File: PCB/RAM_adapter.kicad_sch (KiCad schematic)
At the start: 13 parts, among them J1 #WR, J2 DB25_Plug, U1 HM62256BLP, U2 74LS573

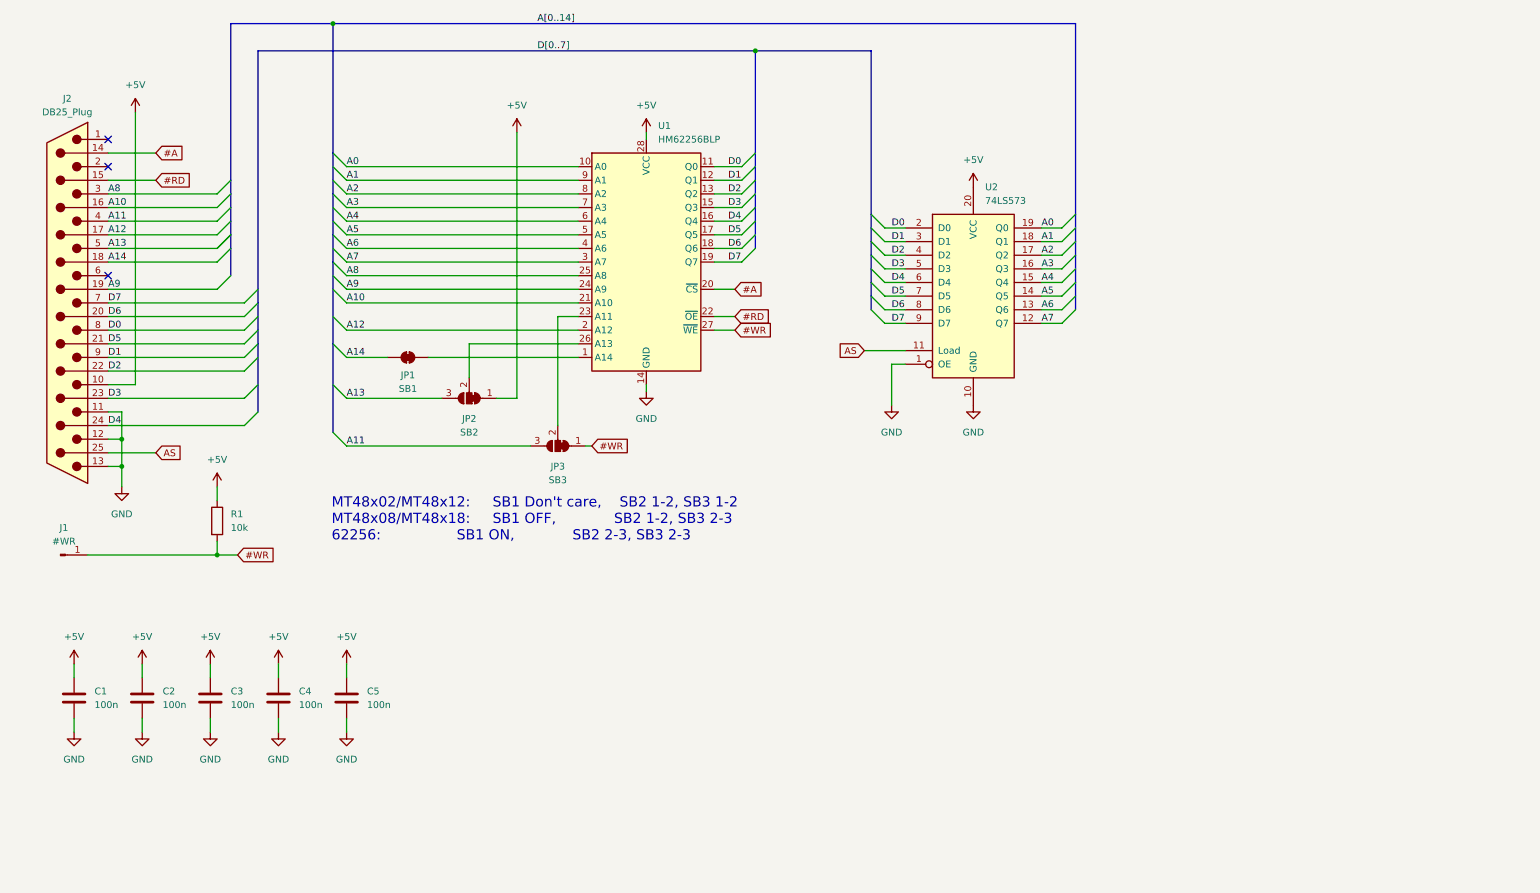
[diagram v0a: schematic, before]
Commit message: Revised RAM adapter PCB
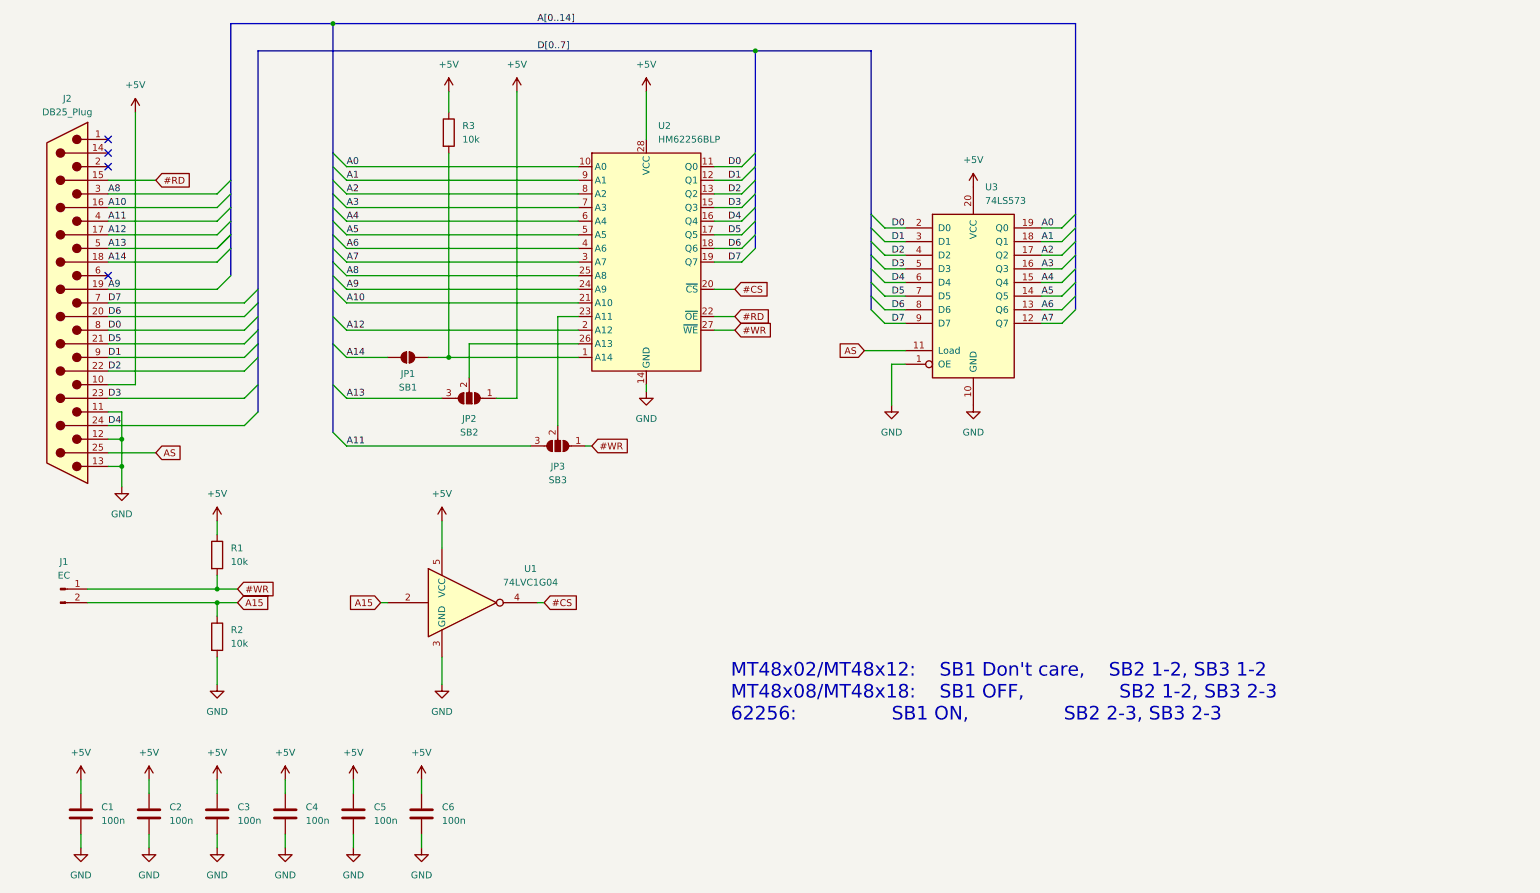
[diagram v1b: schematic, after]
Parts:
- removed J1: #WR, Connector_PinHeader_2.54mm:PinHeader_1x01_P2.54mm_Vertical, symbol Connector:Conn_01x01_Pin
- removed JP1: SB1, Jumper:SolderJumper-2_P1.3mm_Bridged_RoundedPad1.0x1.5mm, symbol Jumper:SolderJumper_2_Bridged
- removed JP2: SB2, Jumper:SolderJumper-3_P1.3mm_Bridged12_RoundedPad1.0x1.5mm_NumberLabels, symbol Jumper:SolderJumper_3_Bridged12
- removed JP3: SB3, Jumper:SolderJumper-3_P1.3mm_Bridged12_RoundedPad1.0x1.5mm_NumberLabels, symbol Jumper:SolderJumper_3_Bridged12
- added C6: 100n, Capacitor_SMD:C_1206_3216Metric_Pad1.33x1.80mm_HandSolder, symbol Device:C
- added J1: EC, Connector_PinHeader_2.54mm:PinHeader_1x02_P2.54mm_Vertical, symbol Connector:Conn_01x02_Pin
- added JP1: SB1, Jumper:SolderJumper-2_P1.3mm_Open_RoundedPad1.0x1.5mm, symbol Jumper:SolderJumper_2_Open
- added JP2: SB2, Jumper:SolderJumper-3_P1.3mm_Open_RoundedPad1.0x1.5mm, symbol Jumper:SolderJumper_3_Open
- added JP3: SB3, Jumper:SolderJumper-3_P1.3mm_Open_RoundedPad1.0x1.5mm, symbol Jumper:SolderJumper_3_Open
- added R2, R3: 10k, Resistor_SMD:R_1206_3216Metric_Pad1.30x1.75mm_HandSolder, symbol Device:R
- added U1: 74LVC1G04, Package_TO_SOT_SMD:SOT-23-5_HandSoldering, symbol 74xGxx:74LVC1G04
- U2: renamed from U1; footprint Package_DIP:DIP-28_W15.24mm -> Socket:DIP_Socket-28_W11.9_W12.7_W15.24_W17.78_W18.5_3M_228-1277-00-0602J
- renumbered U2 to U3
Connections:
- net #WR: now also J1.1 (Pin_1), JP3.1 (A)
- net +5V: now also C6.1, JP2.1 (A), R3.1, U1.5 (VCC)
- net A11: now also JP3.3 (B)
- net A13: now also JP2.3 (B)
- net A14: now also JP1.2 (B)
- net GND: now also C6.2, R2.2, U1.3 (GND)
- net at U2.26 (A13): now also JP2.2 (C)
- net at U2.1 (A14): now also JP1.1 (A), R3.2
- net at U2.23 (A11): now also JP3.2 (C)
- net #A: no longer names the net of J2.14 (P14)
- net #A: no longer U2.20 (~{CS})
- new net #CS: U1.4, U2.20 (~{CS})
- new net A15: J1.2 (Pin_2), R2.1, U1.2
- no-connect marks 3 -> 4
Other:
- moved on the sheet: C1, C2, C3, C4, C5, R1

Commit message: ROM reader project PCBs updated
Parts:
- added D1: Schottky, Diode_SMD:D_SMB_Handsoldering, symbol Device:D_Schottky
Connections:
- net +5V: now also D1.1 (K)
- net GND: now also D1.2 (A)
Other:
- note added: "M48x02/M48x12: SB1 OFF, SB2 1-2, SB3 1-2 M48x08/M48x18: SB1 OFF, SB2 1-2, SB3 2-3 62256: SB1 ON, SB2 2-3, SB3 2-3"
- note removed: "MT48x02/MT48x12: SB1 Don't care, SB2 1-2, SB3 1-2 MT48x08/MT48x18: SB1 OFF, SB2 1-2, SB3 2-3 62256: SB1 ON, SB2 2-3, SB3 2-3"
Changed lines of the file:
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@@
 		)
 	)
+	(wire
+		(pts
+			(xy 129.54 170.18) (xy 129.54 172.72)
+		)
+		(stroke
+			(width 0)
+			(type default)
+		)
+	)
 	(bus
 		(pts
@@
 		)
 	)
+	(wire
+		(pts
+			(xy 129.54 180.34) (xy 129.54 182.88)
+		)
+		(stroke
+			(width 0)
+			(type default)
+		)
+	)
 	(bus
 		(pts
@@
 		)
 	)
-	(text "MT48x02/MT48x12:	SB1 Don't care,	SB2 1-2, SB3 1-2\nMT48x08/MT48x18:	SB1 OFF,				SB2 1-2, SB3 2-3\n62256:				SB1 ON,				SB2 2-3, SB3 2-3"
+	(text "M48x02/M48x12:	SB1 OFF,	SB2 1-2, SB3 1-2\nM48x08/M48x18:	SB1 OFF,	SB2 1-2, SB3 2-3\n62256:			SB1 ON,	SB2 2-3, SB3 2-3"
 		(exclude_from_sim no)
-		(at 171.958 153.924 0)
+		(at 187.452 155.194 0)
 		(effects
 			(font
@@
 	)
 	(symbol
+		(lib_name "GND_1")
+		(lib_id "power:GND")
+		(at 129.54 182.88 0)
+		(unit 1)
+		(exclude_from_sim no)
+		(in_bom yes)
+		(on_board yes)
+		(dnp no)
+		(fields_autoplaced yes)
+		(property "Reference" "#PWR027"
+			(at 129.54 189.23 0)
+			(effects
+				(font
+					(size 1.27 1.27)
+				)
+				(hide yes)
+			)
+		)
+		(property "Value" "GND"
+			(at 129.54 187.96 0)
+			(effects
+				(font
+					(size 1.27 1.27)
+				)
+			)
+		)
+		(property "Footprint" ""
+			(at 129.54 182.88 0)
+			(effects
+				(font
+					(size 1.27 1.27)
+				)
+				(hide yes)
+			)
+		)
+		(property "Datasheet" ""
+			(at 129.54 182.88 0)
+			(effects
+				(font
+					(size 1.27 1.27)
+				)
+				(hide yes)
+			)
+		)
+		(property "Description" "Power symbol creates a global label with name \"GND\" , ground"
+			(at 129.54 182.88 0)
+			(effects
+				(font
+					(size 1.27 1.27)
+				)
+				(hide yes)
+			)
+		)
+		(pin "1"
+		)
+		(instances
+			(project "RAM_adapter"
+				(path "/30f92d58-9d26-4bc0-a717-1ce5049f472c"
+					(reference "#PWR027")
+					(unit 1)
+				)
+			)
+		)
+	)
+	(symbol
 		(lib_name "+5V_1")
 		(lib_id "power:+5V")
@@
 	)
 	(symbol
+		(lib_name "+5V_1")
+		(lib_id "power:+5V")
+		(at 129.54 170.18 0)
+		(unit 1)
+		(exclude_from_sim no)
+		(in_bom yes)
+		(on_board yes)
+		(dnp no)
+		(fields_autoplaced yes)
+		(property "Reference" "#PWR026"
+			(at 129.54 173.99 0)
+			(effects
+				(font
+					(size 1.27 1.27)
+				)
+				(hide yes)
+			)
+		)
+		(property "Value" "+5V"
+			(at 129.54 165.1 0)
+			(effects
+				(font
+					(size 1.27 1.27)
+				)
+			)
+		)
+		(property "Footprint" ""
+			(at 129.54 170.18 0)
+			(effects
+				(font
+					(size 1.27 1.27)
+				)
+				(hide yes)
+			)
+		)
+		(property "Datasheet" ""
+			(at 129.54 170.18 0)
+			(effects
+				(font
+					(size 1.27 1.27)
+				)
+				(hide yes)
+			)
+		)
+		(property "Description" "Power symbol creates a global label with name \"+5V\""
+			(at 129.54 170.18 0)
+			(effects
+				(font
+					(size 1.27 1.27)
+				)
+				(hide yes)
+			)
+		)
+		(pin "1"
+		)
+		(instances
+			(project "RAM_adapter"
+				(path "/30f92d58-9d26-4bc0-a717-1ce5049f472c"
+					(reference "#PWR026")
+					(unit 1)
+				)
+			)
+		)
+	)
+	(symbol
 		(lib_name "GND_1")
 		(lib_id "power:GND")
@@
 					(unit 1)
 				)
+			)
+		)
+	)
+	(symbol
+		(lib_id "Device:D_Schottky")
+		(at 129.54 176.53 270)
+		(unit 1)
+		(exclude_from_sim no)
+		(in_bom yes)
+		(on_board yes)
+		(dnp no)
+		(fields_autoplaced yes)
+		(property "Reference" "D1"
+			(at 132.08 174.9424 90)
+			(effects
+				(font
+					(size 1.27 1.27)
+				)
+				(justify left)
+			)
+		)
+		(property "Value" "Schottky"
+			(at 132.08 177.4824 90)
+			(effects
+				(font
+					(size 1.27 1.27)
+				)
+				(justify left)
+			)
+		)
+		(property "Footprint" "Diode_SMD:D_SMB_Handsoldering"
+			(at 129.54 176.53 0)
+			(effects
+				(font
+					(size 1.27 1.27)
+				)
+				(hide yes)
+			)
+		)
+		(property "Datasheet" "~"
+			(at 129.54 176.53 0)
+			(effects
+				(font
+					(size 1.27 1.27)
+				)
+				(hide yes)
+			)
+		)
+		(property "Description" "Schottky diode"
+			(at 129.54 176.53 0)
+			(effects
+				(font
+					(size 1.27 1.27)
+				)
+				(hide yes)
+			)
+		)
+		(pin "1"
+		)
+		(pin "2"
+		)
+		(instances
+			(project ""
+				(path "/30f92d58-9d26-4bc0-a717-1ce5049f472c"
+					(reference "D1")
+					(unit 1)
+				)

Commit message: Minor changes in text placement on PCB, comments. Revision updated to B
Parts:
- J1: value EC -> RAM ADAPTER EXT
- J2: value DB25_Plug -> ROM
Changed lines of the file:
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@@
 	(title_block
 		(title "ROM reader RAM adapter")
-		(date "2024-08-17")
-		(rev "A")
+		(date "2025-01-22")
+		(rev "B")
 		(company "trwgQ26xxx")
 	)
@@
 			)
 		)
-		(property "Value" "DB25_Plug"
+		(property "Value" "ROM"
 			(at 48.26 45.72 0)
 			(effects
@@
 		(on_board yes)
 		(dnp no)
-		(fields_autoplaced yes)
 		(property "Reference" "J1"
 			(at 47.625 129.54 0)
@@
 			)
 		)
-		(property "Value" "EC"
+		(property "Value" "RAM ADAPTER EXT"
 			(at 47.625 132.08 0)
 			(effects
